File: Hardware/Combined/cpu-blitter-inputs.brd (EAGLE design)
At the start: 177.8 x 152.4 mm, 149 parts, among them IC1 74S08N, IC12 74S08N, IC16 7404N, IC18 7432N, IC2 7404N, IC20 7430N, IC21 7400N, IC31 7400N, IC32 7432N, IC4 7404N, IC5 7400N, IC53 7404N, IC54 74LS07N, IC7 74S08N, IC9 74LS74N, J2 TX25-40P-6ST-H1E, U1 W65C02SP, U2 VIA

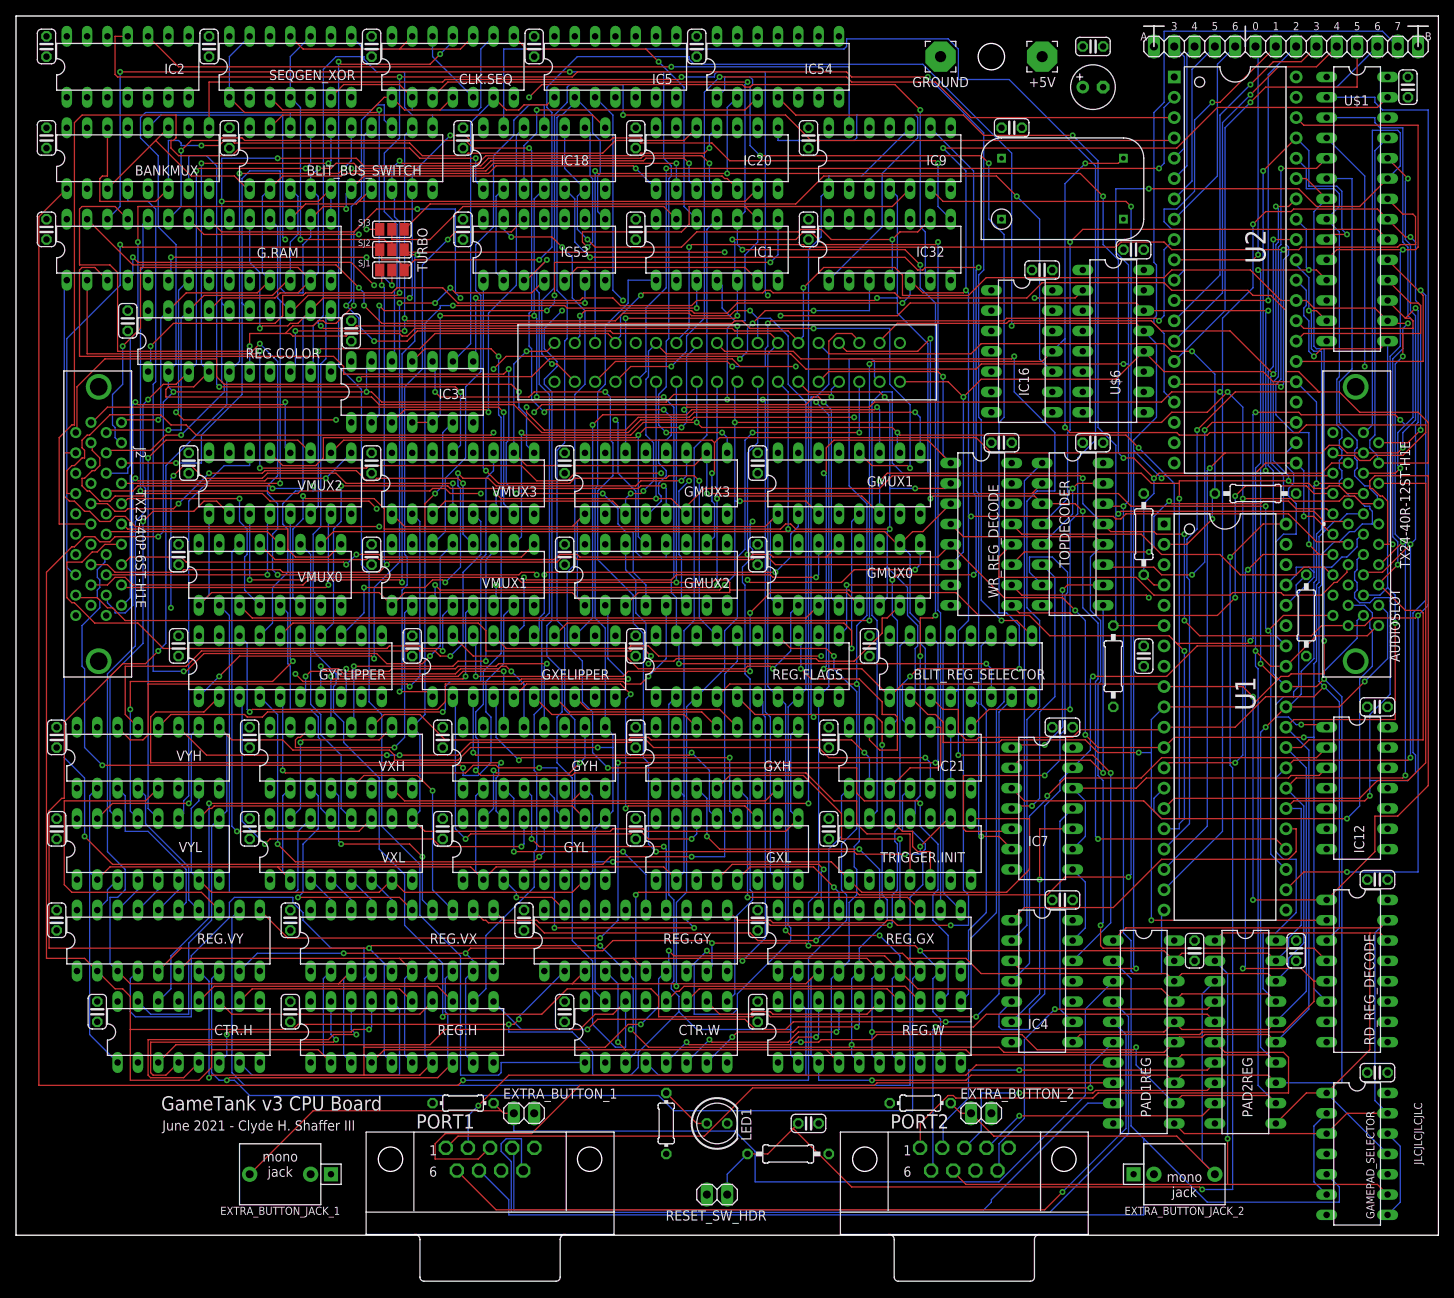
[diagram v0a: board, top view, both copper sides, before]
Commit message: Updates to combined board inc. new blitter features
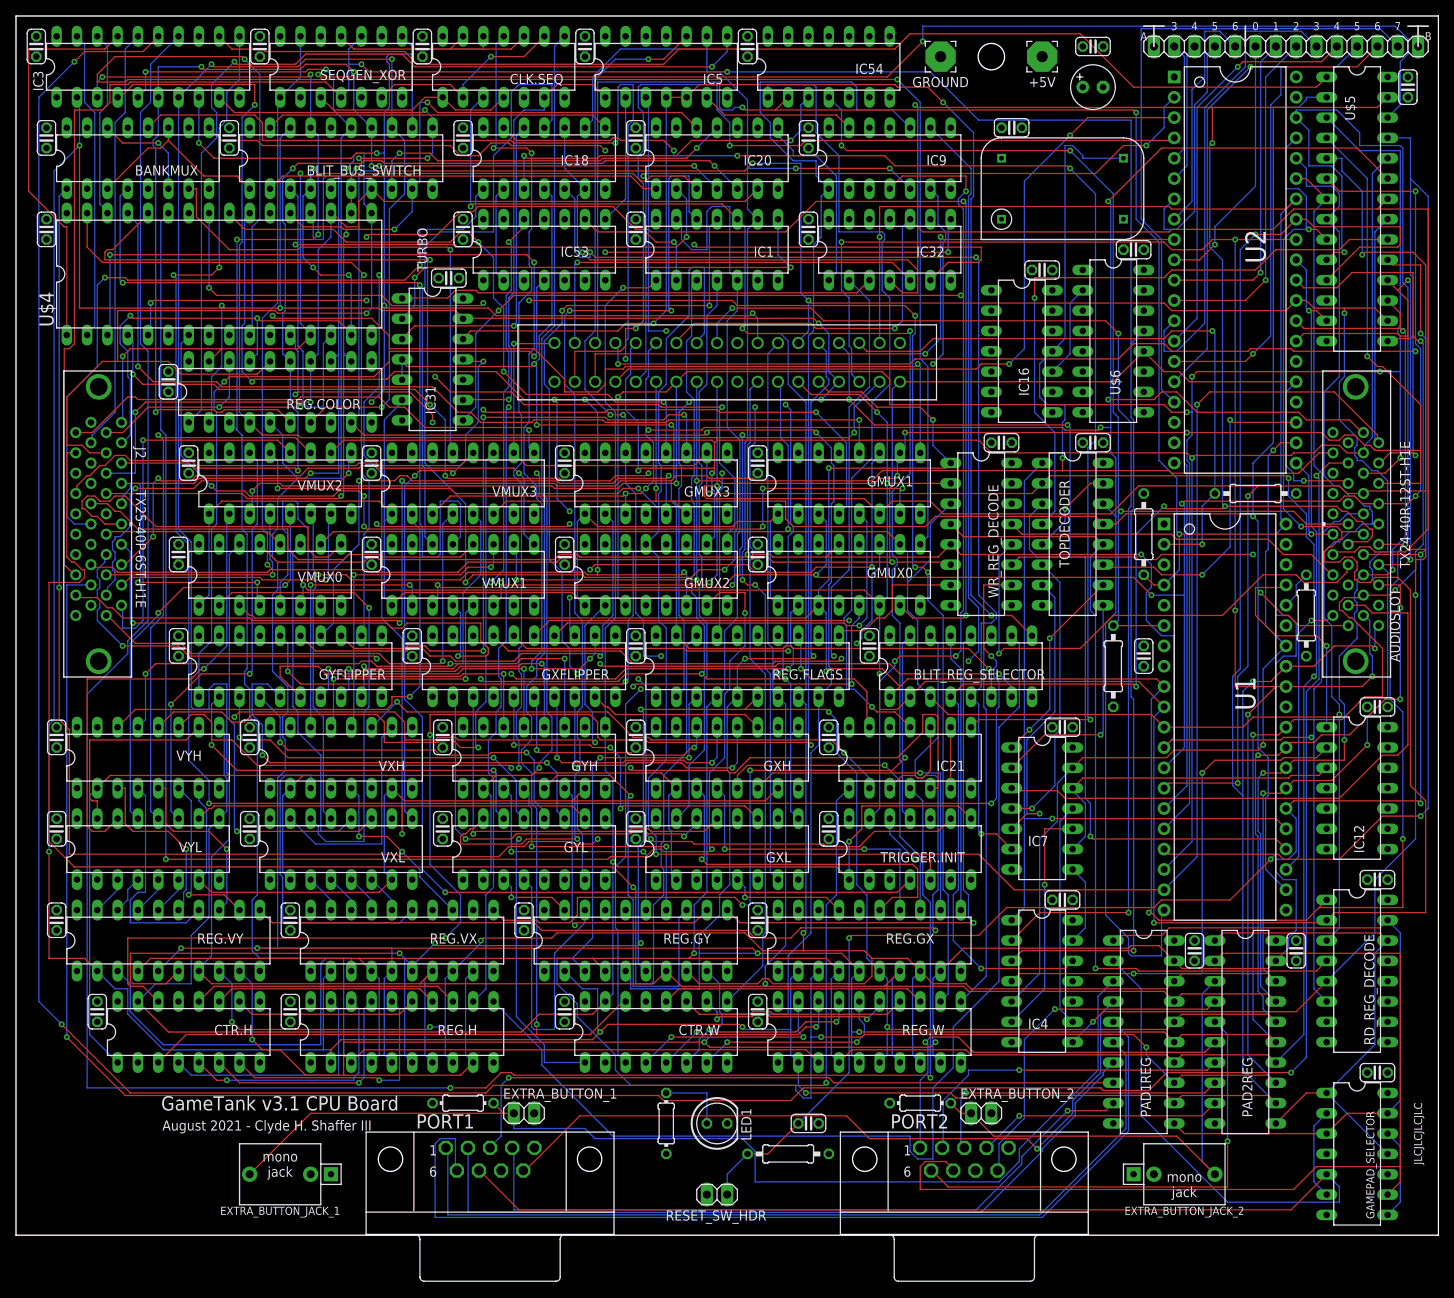
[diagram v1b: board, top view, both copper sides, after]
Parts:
- removed G.RAM: SRAM_32K, 000_mychips2:DIL28-3
- removed IC2: 7404N, 74xx-us:DIL14
- removed SJ1, SJ2, SJ3: (no value), jumper:SJ_2
- removed U$1: SRAM_08K, 000_mychips2:DIL28-3
- added IC3: 74HC573N, 74xx-us:DIL20
- added U$4: AS6C4008, 0_gametankparts:DIL32
- added U$5: SRAM_32K, 0_gametankparts:DIL28-3
- moved C54 13.9 mm to (54.1, 94.2), turned to 180 degrees
- moved C53 9.16 mm to (19.1, 81.3)
- moved REG.COLOR 8.13 mm to (33.0, 80.0)
- moved C19 6.35 mm to (71.1, 123.2)
- moved C18 6.35 mm to (30.5, 123.2)
- moved CLK.SEQ 6.35 mm to (61.0, 120.7)
- moved SEQGEN_XOR 6.35 mm to (40.6, 120.7)
- moved C12 6.35 mm to (50.8, 123.2)
- moved C17 6.35 mm to (91.4, 123.2)
- moved IC5 6.35 mm to (81.3, 120.7)
- moved IC54 6.35 mm to (101.6, 120.7)
- moved IC31 4.79 mm to (52.1, 84.1), turned to 270 degrees
- moved C50 1.27 mm to (2.54, 123.2)
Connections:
- net TRANSEN renamed !TRANSEN
- net VIDPAGE renamed VID_OUT_PAGE
- removed net !OE2: IC32.10
- removed net AUD_WAVE_N: AUDIOSLOT.8, WR_REG_DECODE.10
- removed net GRAMBANK: G.RAM.1, REG.FLAGS.16
- removed net N$34: IC1.6, IC53.5
- removed net P1LONG: CLK.SEQ.8, IC1.12
- new net !AUD_NMI: AUDIOSLOT.16
- new net !TILEMODE: IC1.13, IC1.5, REG.FLAGS.15
- new net AUD_RESET: AUDIOSLOT.17
- new net AUD_SAMP_RATE_SEL: AUDIOSLOT.7
- new net GA14: GXFLIPPER.12, U$4.3
- new net GA15: GYFLIPPER.12, U$4.31
- new net GA16: IC3.19, U$4.2
- new net GA17: IC3.18, U$4.30
- new net GA18: IC3.17, U$4.1
- new net GRAM_PAGE_SEL: IC3.11, WR_REG_DECODE.10
- new net GX-CARRY?: GXL.15, IC1.4
- new net GY-CARRY?: GYL.15, IC1.12
- new net N$150: GXH.6, REG.GX.12
- new net N$151: GYH.6, REG.GY.12
- new net N$84: REG.VY.12, VYH.6
- new net RAM_PG_0: IC3.13, U$5.26
- new net RAM_PG_1: IC3.12, U$5.1
- new net VDD: U$4.32
- new net VSS: U$4.16
- net !CLK28: no longer SJ3.3
- net !RAMSEL: now also U$5.20; no longer U$1.20
- net !RE2: now also IC32.10, U$5.22; no longer U$1.22
- net !WE2: now also U$5.27; no longer U$1.27
- net !WRAP_X: now also IC3.15; no longer REG.VX.12
- net !WRAP_Y: now also IC3.14; no longer REG.VY.12
- net A0: now also U$5.10; no longer U$1.10
- net A1: now also U$5.9; no longer U$1.9
- net A10: now also U$5.21; no longer U$1.21
- net A11: now also U$5.23; no longer U$1.23
- net A12: now also U$5.2; no longer U$1.2
- net A2: now also U$5.8; no longer U$1.8
- net A3: now also U$5.7; no longer U$1.7
- net A4: now also U$5.6; no longer U$1.6
- net A5: now also U$5.5; no longer U$1.5
- net A6: now also U$5.4; no longer U$1.4
- net A7: now also U$5.3; no longer U$1.3
- net A8: now also U$5.25; no longer U$1.25
- net A9: now also U$5.24; no longer U$1.24
- net AUD_SQ1_N: no longer AUDIOSLOT.17
- net AUD_SQ1_X: no longer AUDIOSLOT.16
- net AUD_WAVE_X: no longer AUDIOSLOT.7
- net CLK14: no longer SJ2.3
- net CLK3_5: now also SEQGEN_XOR.1, SEQGEN_XOR.13; no longer SJ1.1
- net CLK7: now also SEQGEN_XOR.10, SEQGEN_XOR.4; no longer SJ1.3, SJ2.1
- net COLORFILL: now also IC5.10, REG.FLAGS.16; no longer IC1.5, REG.GX.12
- net D0: now also IC3.2, U$5.11; no longer U$1.11
- net D1: now also IC3.3, U$5.12; no longer U$1.12
- net D2: now also IC3.4, U$5.13; no longer U$1.13
- net D3: now also IC3.5, U$5.15; no longer U$1.15
- net D4: now also IC3.6, U$5.16; no longer U$1.16
- net D5: now also IC3.7, U$5.17; no longer U$1.17
- net D6: now also IC3.8, U$5.18; no longer U$1.18
- net D7: now also IC3.9, U$5.19; no longer U$1.19
- net DD0: now also U$4.13; no longer G.RAM.11
- net DD1: now also U$4.14; no longer G.RAM.12
- net DD2: now also U$4.15; no longer G.RAM.13
- net DD3: now also U$4.17; no longer G.RAM.15
- net DD4: now also U$4.18; no longer G.RAM.16
- net DD5: now also U$4.19; no longer G.RAM.17
- net DD6: now also U$4.20; no longer G.RAM.18
- net DD7: now also U$4.21; no longer G.RAM.19
- net GND: now also IC3.1, IC3.10, U$4.22, U$5.14; no longer G.RAM.14, G.RAM.20, IC2.7, U$1.14
- net GX-CARRY: now also IC1.6; no longer GXL.15
- net GY-CARRY: now also IC1.11; no longer GYL.15
- net N$1: now also U$4.12; no longer G.RAM.10
- net N$10: now also U$4.26; no longer G.RAM.24
- net N$11: now also U$4.23; no longer G.RAM.21
- net N$12: now also U$4.25; no longer G.RAM.23
- net N$13: now also U$4.4; no longer G.RAM.2
- net N$14: now also U$4.28; no longer G.RAM.26
- net N$17: now also U$4.29; no longer G.RAM.27
- net N$18: now also U$4.24; no longer G.RAM.22
- net N$2: now also U$4.11; no longer G.RAM.9
- net N$3: now also U$4.10; no longer G.RAM.8
- net N$4: now also U$4.9; no longer G.RAM.7
- net N$41: now also IC5.8; no longer IC53.6
- net N$5: now also U$4.8; no longer G.RAM.6
- net N$6: now also U$4.7; no longer G.RAM.5
- net N$7: now also U$4.6; no longer G.RAM.4
- net N$8: now also U$4.5; no longer G.RAM.3
- net N$83: now also REG.VX.12, VXH.6; no longer SEQGEN_XOR.10, SEQGEN_XOR.4, SJ2.2
- net N$85: now also GXFLIPPER.9, GXH.11; no longer IC1.13, SJ3.2
- net N$88: now also IC5.6; no longer IC2.10
- net N$89: now also GYFLIPPER.9, GYH.11; no longer SEQGEN_XOR.1, SEQGEN_XOR.13, SJ1.2
- net N$9: now also U$4.27; no longer G.RAM.25
- net P1: now also CLK.SEQ.8; no longer IC1.11
- net RUNNING: now also IC5.9; no longer IC1.4
- net TRIGGER-SELECT: now also IC5.4, IC5.5; no longer IC2.11
- net VCC: now also IC3.20, U$5.28; no longer G.RAM.28, IC2.14, SJ3.1, U$1.26, U$1.28
- net VRAMBANK: now also IC3.16; no longer REG.FLAGS.15
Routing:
- net GRAM_PAGE_SEL: track 0.00 -> 234.0 mm, vias 0 -> 5
- net !WRAP_X: track 65.2 -> 272.8 mm, vias 1 -> 3
- net GRAMBANK: track 180.8 -> 0.00 mm, vias 2 -> 0
- net RAM_PG_0: track 0.00 -> 168.5 mm, vias 0 -> 2
- net RAM_PG_1: track 0.00 -> 144.7 mm
- net !WRAP_Y: track 146.4 -> 280.7 mm, vias 0 -> 2
- net D1: track 543.6 -> 673.7 mm, vias 9 -> 13
- net GA14: track 0.00 -> 127.3 mm, vias 0 -> 4
- net GY-CARRY?: track 0.00 -> 125.4 mm, vias 0 -> 3
- net N$3: track 110.9 -> 216.4 mm
- net N$125: track 209.3 -> 104.3 mm
- net CLK14: track 227.9 -> 331.8 mm, vias 6 -> 3
- net !CLK28: track 111.2 -> 11.7 mm, vias 2 -> 0
- net VID_OUT_PAGE: track 94.4 -> 190.7 mm
- net D4: track 516.3 -> 611.2 mm, vias 7 -> 16
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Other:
- board text added: "August 2021 - Clyde H. Shaffer III"
- board text added: "GameTank v3.1 CPU Board"
- board text removed: "GameTank v3 CPU Board"
- board text removed: "June 2021 - Clyde H. Shaffer III"
